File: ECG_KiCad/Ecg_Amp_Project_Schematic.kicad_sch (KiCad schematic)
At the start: 32 parts, among them U1 TL084, U2 TL084

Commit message: Second original
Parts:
- Opamp_Dual: value ~ -> (none)

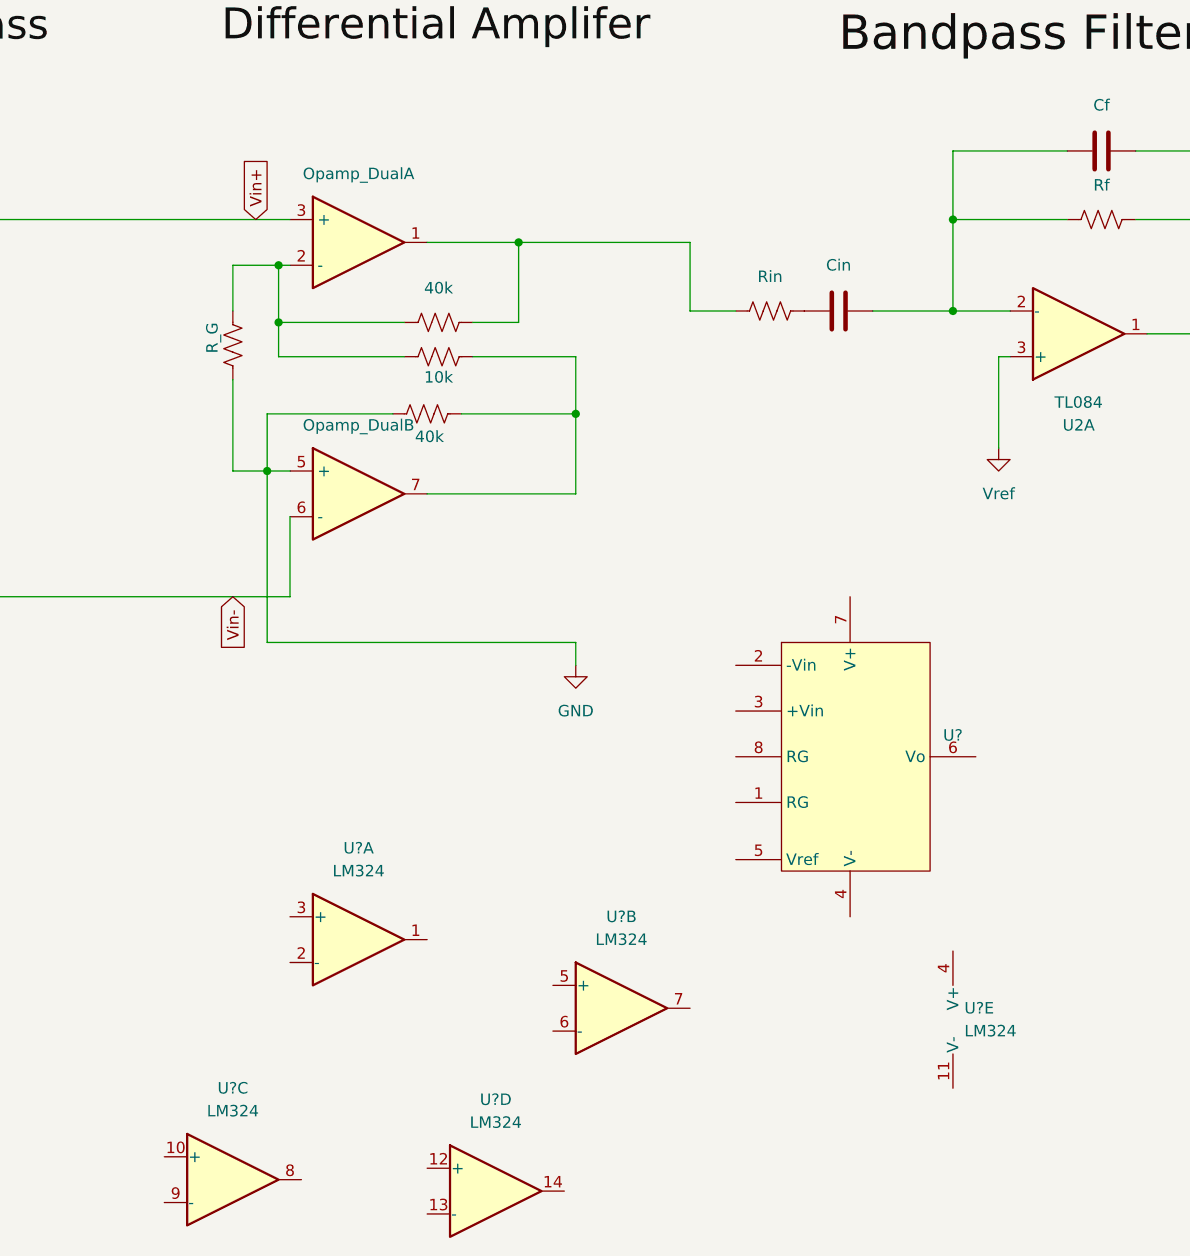
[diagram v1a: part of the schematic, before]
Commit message: Added INA126p symbol, and added Vo pin plus numeration for pins
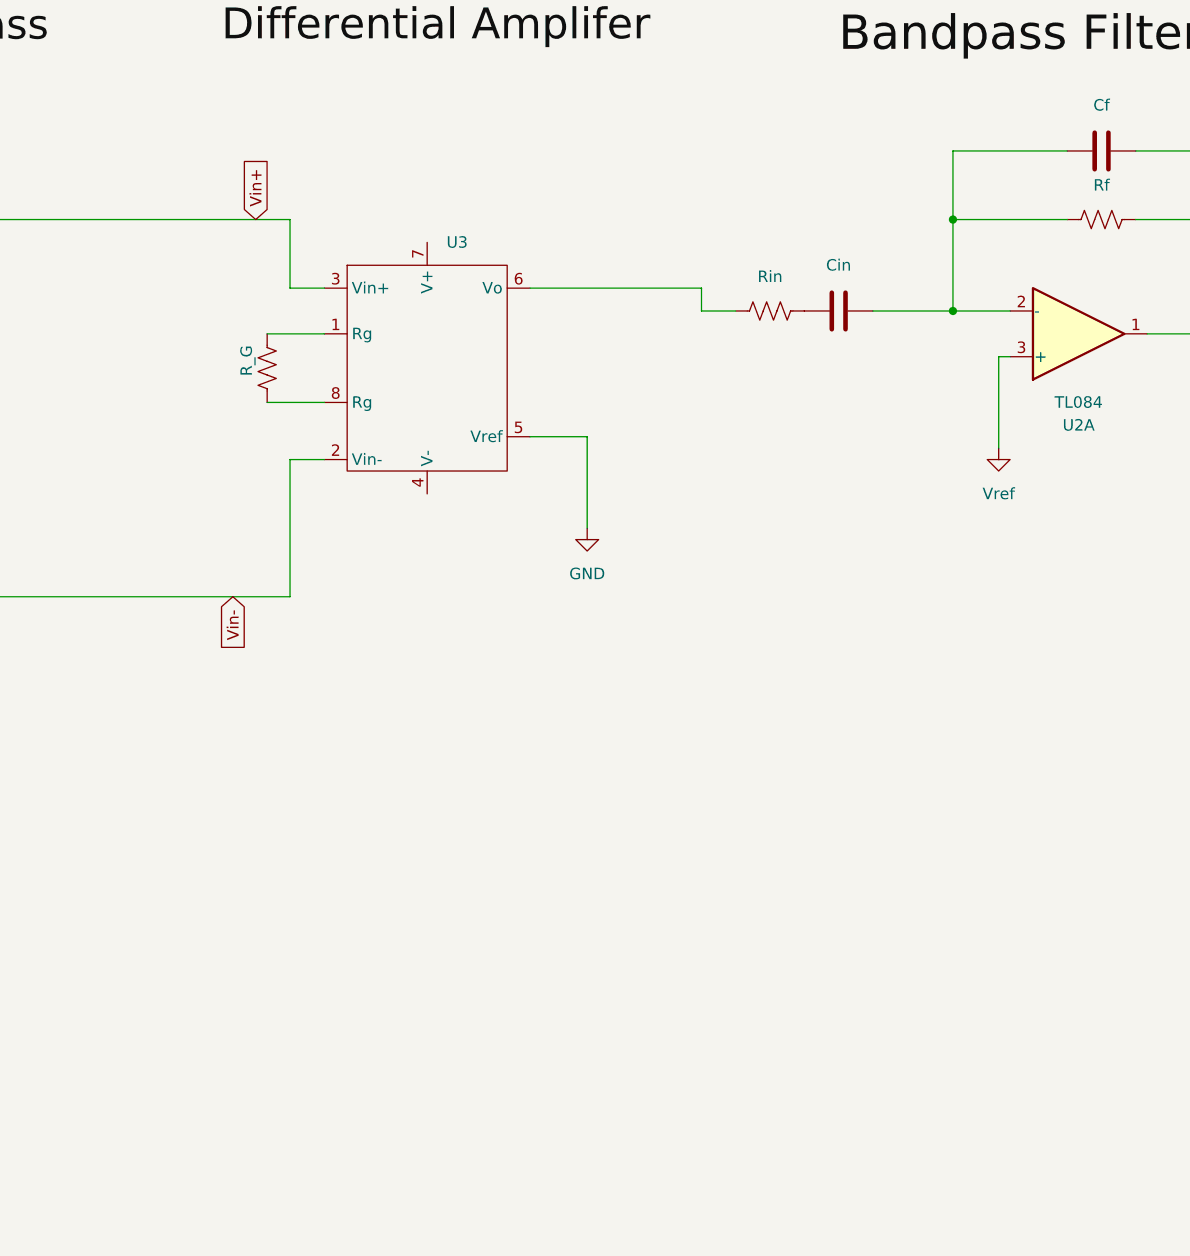
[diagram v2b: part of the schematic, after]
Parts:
- removed Opamp_Dual: Opamp_Dual, symbol Device:Opamp_Dual
- removed R? (x2): 40k, symbol Device:R_US
- removed R?: 10k, symbol Device:R_US
- removed U? (x5): LM324, symbol Amplifier_Operational:LM324
- removed U?: ~, symbol ECG_EE4810:INA126P
- added U3: (no value), symbol ECG_4810_Symbols:INA126p
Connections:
- net GND: now also U3.5 (Vref); no longer R?.2
- net Vin+: now also U3.3 (Vin+)
- net Vin-: now also U3.2 (Vin-)
- net at R?.1: now also U3.1 (Rg)
- net at Rin.1: now also U3.6 (Vo)
- new net: R?.2, U3.8 (Rg)

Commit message: Finished Version 1 of circuit schematic
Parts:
- added BT1, BT2: Battery_Cell, symbol Device:Battery_Cell
- added J1: Screw_Terminal_01x02, symbol Connector:Screw_Terminal_01x02
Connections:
- net GND: now also BT1.2 (-), BT2.1 (+)
- net VDD: now reaches U3.4 (V-)
- net VDD: now also U1.4 (V+), U2.4 (V+), BT2.2 (-), J1.2 (Pin_2)
- net VCC: now reaches U3.7 (V+)
- net VCC: now also U1.11 (V-), U2.11 (V-), BT1.1 (+), J1.1 (Pin_1)
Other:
- note added: "Dual supply power system"

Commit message: Added INA126P dimensions for PCB footprints
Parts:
- added unit 2 of U1
- added unit 5 of U2
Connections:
- net GND: now also U1.5 (+); no longer U1.5 (+)
- net VCC: now also U2.11 (V-); no longer U2.11 (V-)
- net VDD: now also U2.4 (V+); no longer U2.4 (V+)
- net Vin-: now also U1.7; no longer U1.7
- net at Cin.2, Rf.1: now also U1.6 (-); no longer U1.6 (-)

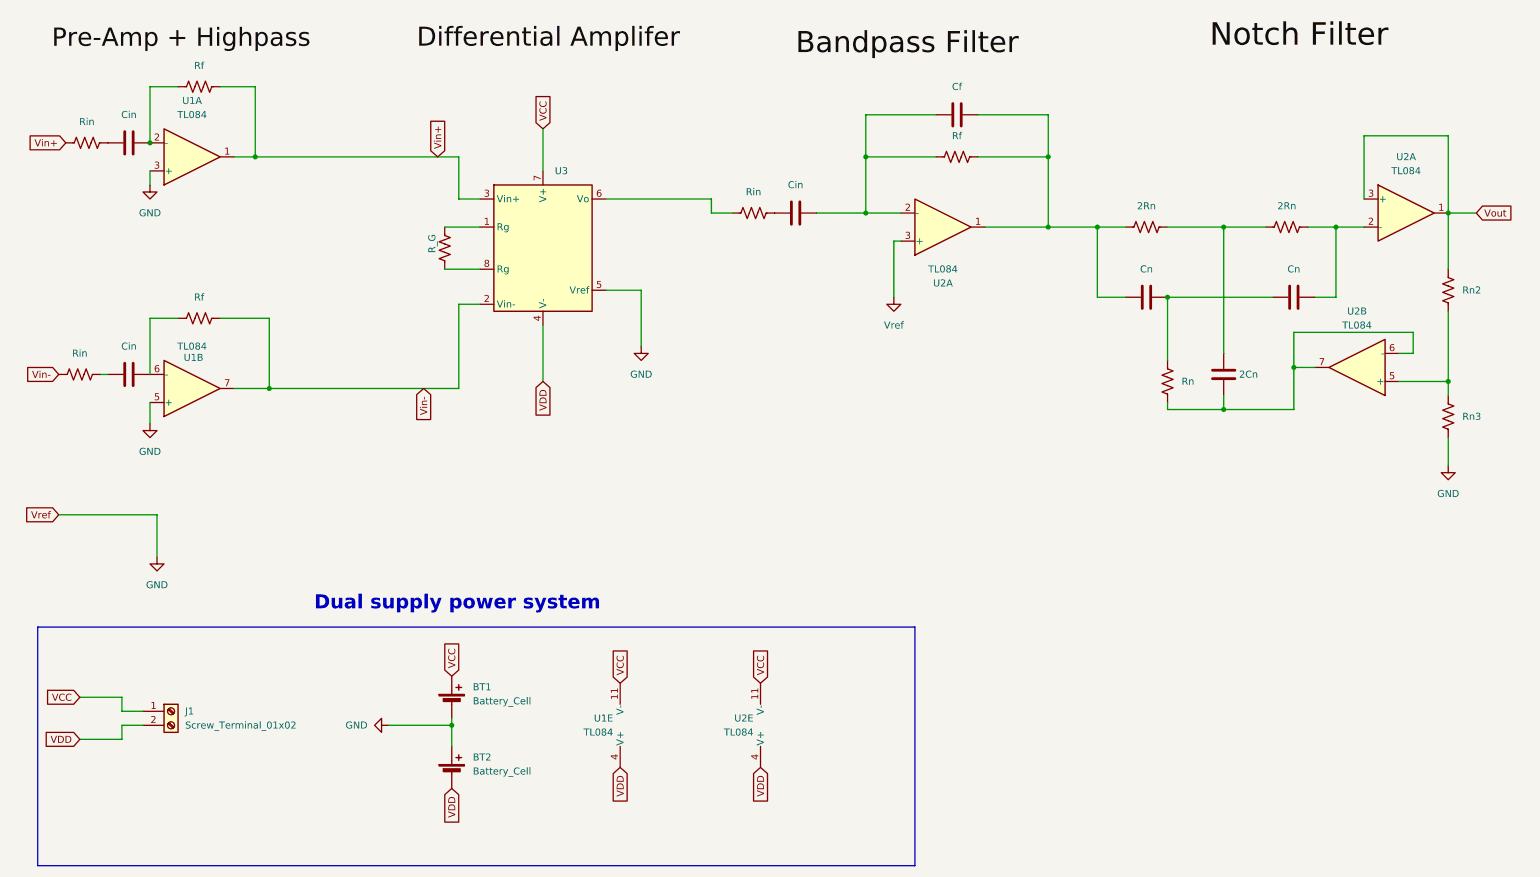
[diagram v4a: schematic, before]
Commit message: Fixed for ERC errors, added our footprints to the PCB editor, fixed INA127P footprint
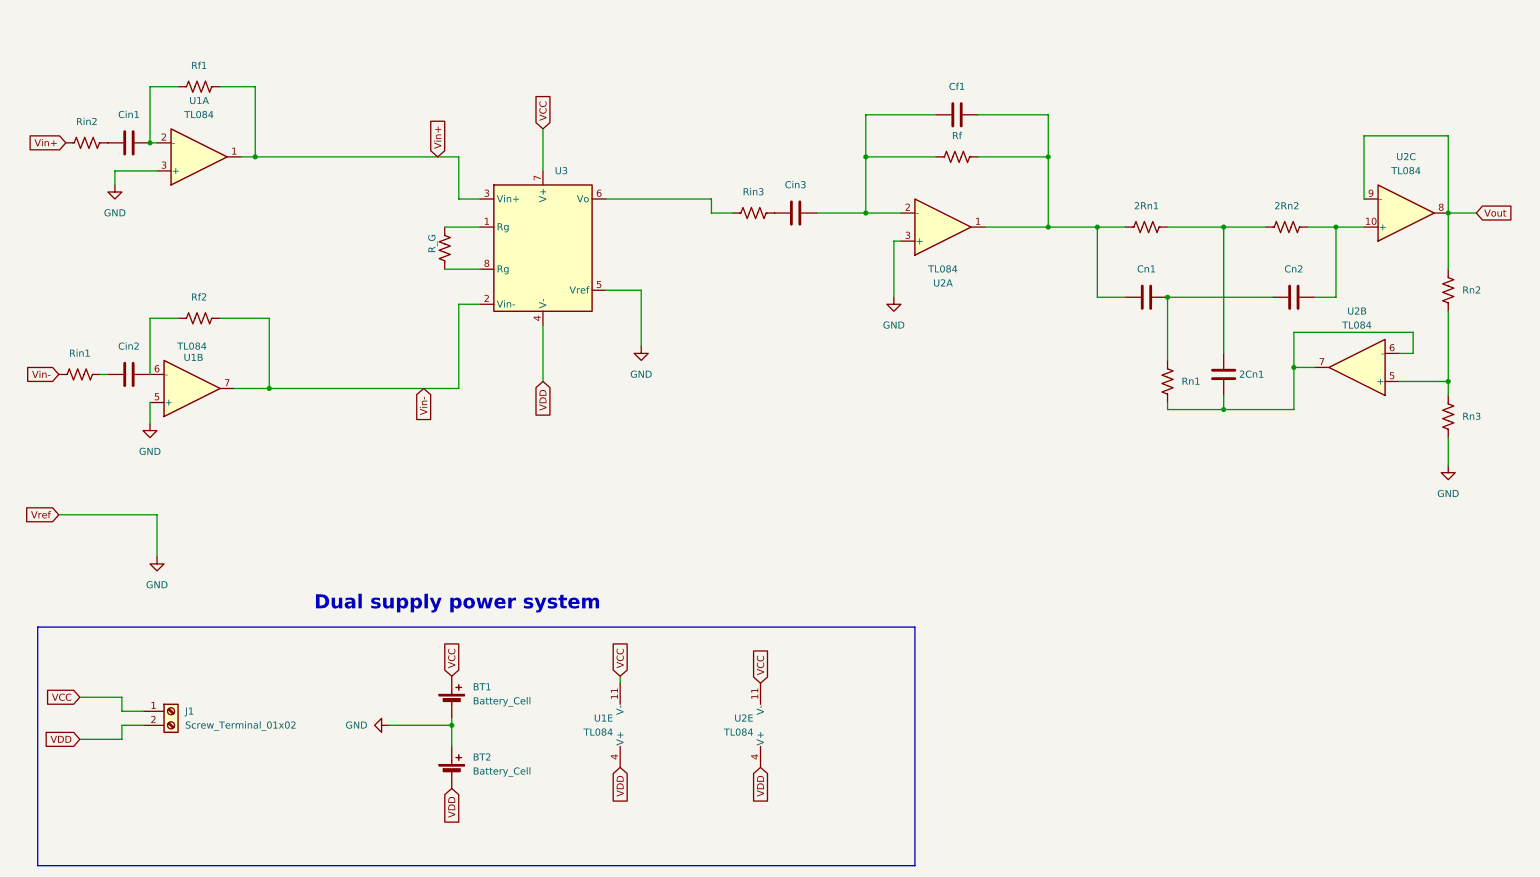
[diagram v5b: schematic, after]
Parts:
- removed U2: TL084, symbol Amplifier_Operational:TL084
- added unit 3 of U2
- J1: footprint (none) -> Connector_Phoenix_MC_HighVoltage:PhoenixContact_MCV_1,5_2-G-5.08_1x02_P5.08mm_Vertical
- U3: footprint (none) -> ECG_4810_Footprints:INA126P
- gave numbers to parts that had none: 2
- renumbered 2Cn to 2Cn1, 2Rn to 2Rn1, 2Rn to 2Rn2, Cf to Cf1, Cin to Cin1, Cin to Cin2, Cin to Cin3, Cn to Cn1, Cn to Cn2, Rf to Rf1, Rf to Rf2, Rin to Rin1, Rin to Rin2, Rin to Rin3, Rn to Rn1
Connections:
- net Vout: now also U2.8, U2.9 (-)
- net at 2Rn2.2, Cn2.2: now also U2.10 (+)
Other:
- moved on the sheet: U1A
